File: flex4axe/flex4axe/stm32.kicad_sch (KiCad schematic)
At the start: 30 parts, among them J3 USB_C_Receptacle_USB2.0, J4 Conn_01x06, J5 Conn_01x10, J5 SWD, M2 Fan_4pin, U1 ${REFERENCE}, U3 STM32L052K6Tx, U39 TXU0101

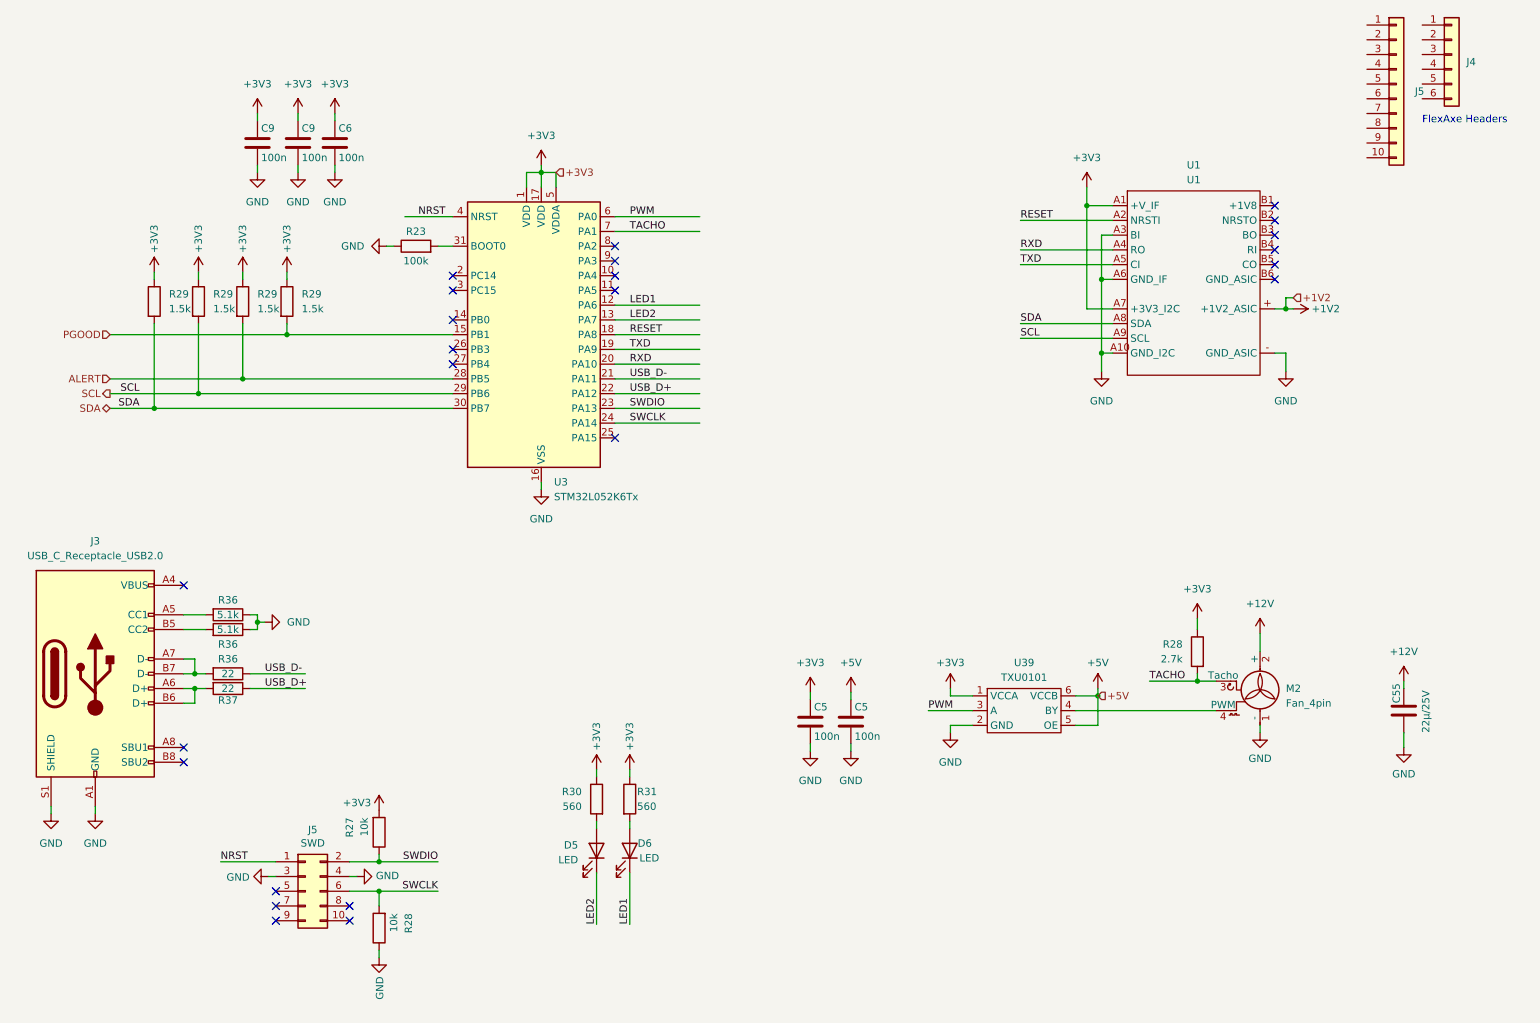
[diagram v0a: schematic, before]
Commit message: forgot to push the 4 flex version back then
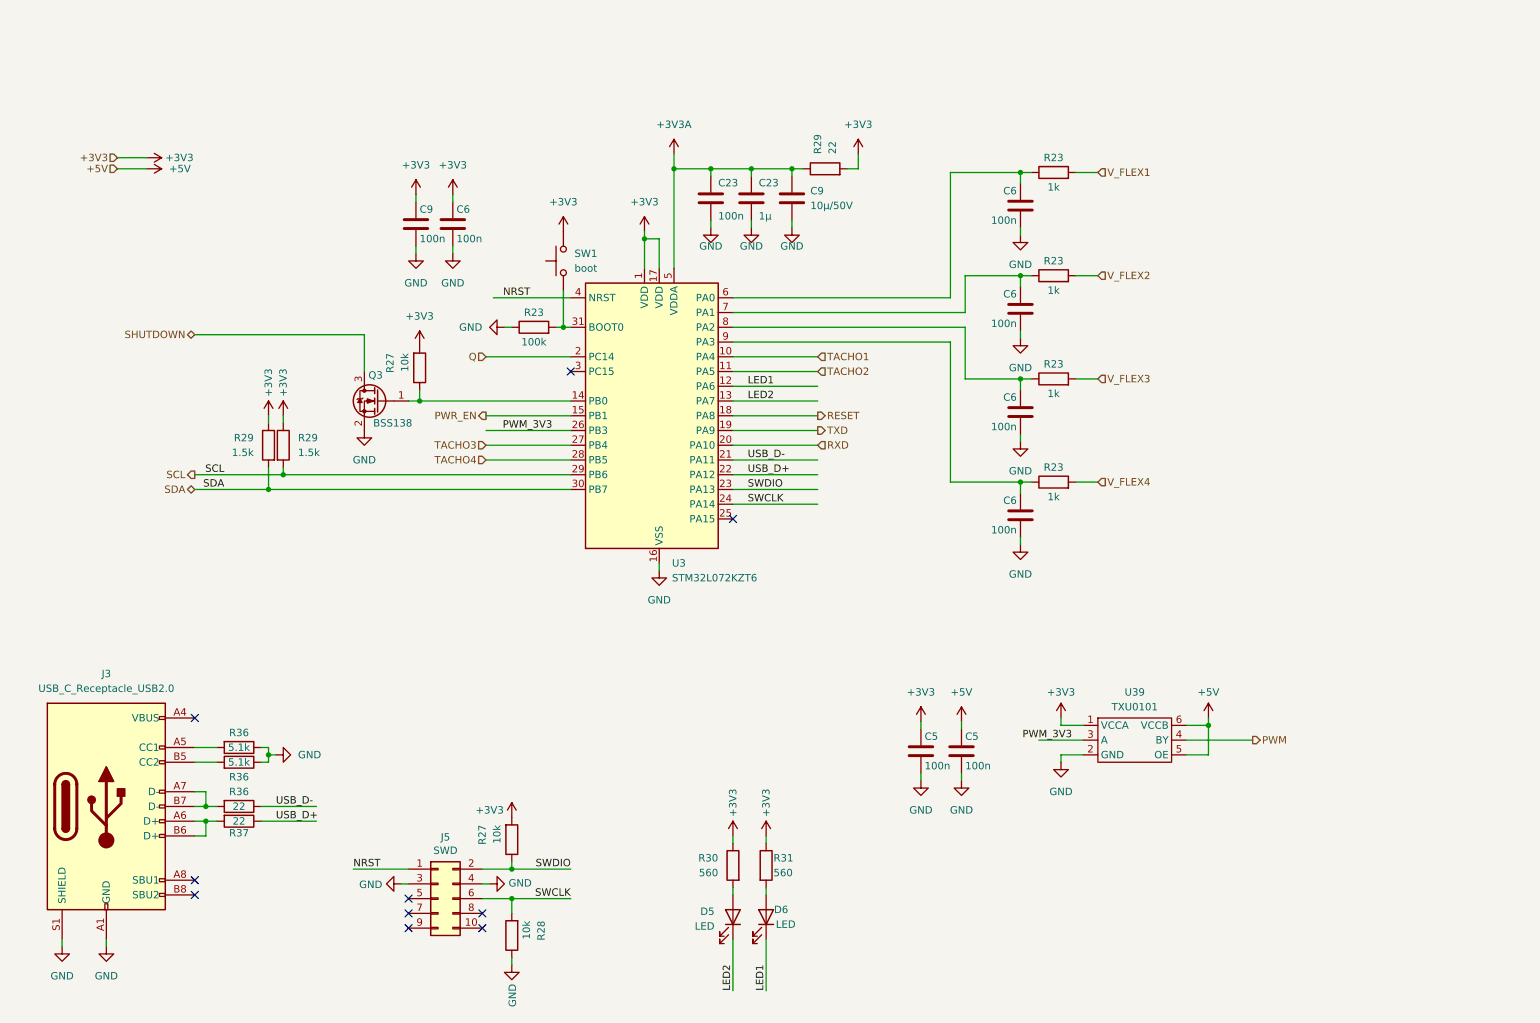
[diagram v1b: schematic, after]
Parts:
- removed C5 (x2), C6, C9 (x2): 100n, Capacitor_SMD:C_0805_2012Metric, symbol vfd1-rescue:C
- removed C55: 22µ/25V, Capacitor_SMD:C_1210_3225Metric, symbol Device:C
- removed J4: Conn_01x06, symbol Connector_Generic:Conn_01x06
- removed J5: Conn_01x10, symbol Connector_Generic:Conn_01x10
- removed M2: Fan_4pin, Connector:FanPinHeader_1x04_P2.54mm_Vertical, symbol Motor:Fan_4pin
- removed R23: 100k, Resistor_SMD:R_0805_2012Metric, symbol Device:R
- removed R27: 10k, Resistor_SMD:R_0805_2012Metric, symbol dwc-hat-rescue:R-Device
- removed R28: 2.7k, Resistor_SMD:R_0805_2012Metric, symbol Device:R
- removed R29 (x4): 1.5k, Resistor_SMD:R_0805_2012Metric, symbol Device:R
- removed R36: 22, Resistor_SMD:R_0805_2012Metric, symbol clock-rescue:R
- removed R36 (x2): 5.1k, Resistor_SMD:R_0805_2012Metric, symbol clock-rescue:R
- removed U1: ${REFERENCE}, myfootprints:FLEXAXE, symbol mylib7:FLEXAXE
- added C23: 1µ, Capacitor_SMD:C_0805_2012Metric, symbol Device:C
- added C23: 100n, Capacitor_SMD:C_0805_2012Metric, symbol Device:C
- added C5 (x2), C6 (x5), C9: 100n, Capacitor_SMD:C_0805_2012Metric, symbol vfd1-rescue:C
- added C9: 10µ/50V, Capacitor_SMD:C_1206_3216Metric, symbol Device:C
- added Q3: BSS138, Package_TO_SOT_SMD:SOT-23, symbol Transistor_FET:BSS138
- added R23 (x4): 1k, Resistor_SMD:R_0805_2012Metric, symbol Device:R
- added R23: 100k, Resistor_SMD:R_0805_2012Metric, symbol Device:R
- added R27 (x2): 10k, Resistor_SMD:R_0805_2012Metric, symbol dwc-hat-rescue:R-Device
- added R29: 22, Resistor_SMD:R_0805_2012Metric, symbol Device:R
- added R29 (x2): 1.5k, Resistor_SMD:R_0805_2012Metric, symbol Device:R
- added R36 (x2): 5.1k, Resistor_SMD:R_0805_2012Metric, symbol clock-rescue:R
- added R36: 22, Resistor_SMD:R_0805_2012Metric, symbol clock-rescue:R
- added SW1: boot, Button_Switch_SMD:SW_Push_1P1T_NO_CK_KMR2, symbol Switch:SW_Push
- J5: Distributor (none) -> X
- U3: value STM32L052K6Tx -> STM32L072KZT6; Manufacturer STM32L052K8T6 -> STM32L072KZT6; OrderNr 497-14904-ND -> 497-19668-ND
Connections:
- net +3V3: now also C5.1, C6.1, C9.1, R27.2, R27.2, R29.1, R29.1, R29.2, SW1.2; no longer U3.5 (VDDA)
- net +5V: now also C5.1
- net GND: now also C23.2, C23.2, C5.2, C5.2, C6.2, C6.2, C6.2, C6.2, C6.2, C9.2, C9.2, Q3.2 (S), R23.1, R36.1, R36.1
- net PWM: now also U39.4 (BY); no longer U3.6 (PA0), U39.3 (A)
- net SCL: now also R29.2
- net SDA: now also R29.2
- net SWDIO: now also R27.1
- net USB_D-: now also R36.1
- net at U3.31 (BOOT0): now also R23.2, SW1.1
- net at J3.A5 (CC1): now also R36.2
- net at J3.A7 (D-), J3.B7 (D-): now also R36.2
- net at J3.B5 (CC2): now also R36.2
- net TACHO1: now reaches U3.10 (PA4)
- net TACHO2: now reaches U3.11 (PA5)
- net at U3.14 (PB0): now also Q3.1 (G), R27.1
- net Q: now reaches U3.2 (PC14)
- net PWM_3V3: now reaches U3.26 (PB3)
- net PWM_3V3: now also U39.3 (A)
- net TACHO3: now reaches U3.27 (PB4)
- net at U3.8 (PA2): now also C6.1, R23.1
- net at U3.9 (PA3): now also C6.1, R23.1
- net ALERT renamed TACHO4
- net PGOOD renamed PWR_EN
- net TACHO: no longer names the net of U3.7 (PA1)
- net TACHO: now also C6.1, R23.1
- new net: C6.1, R23.1, U3.6 (PA0)
- new net +3V3A: C23.1, C23.1, C9.1, R29.1, U3.5 (VDDA)
- new net SHUTDOWN: Q3.3 (D)
- new net V_FLEX1: R23.2
- new net V_FLEX2: R23.2
- new net V_FLEX3: R23.2
- new net V_FLEX4: R23.2
- no-connect marks 24 -> 10
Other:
- note removed: "FlexAxe Headers"
